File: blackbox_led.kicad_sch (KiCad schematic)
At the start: 26 parts

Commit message: refactor labels U and assigned resistance footprint
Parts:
- D10, D11, D12, D3, D4, D5: value LED -> NCD0603R3
- D6: renamed from D8; value LED -> NCD0603R3
- D7: renamed from D6; value LED -> NCD0603R3
- D8: renamed from D7; value LED -> NCD0603R3
- D9: renamed from D13; value LED -> NCD0603R3
- R28, R29, R30, R31, R32, R33, R34, R35, R36, R37, R38, R39: footprint (none) -> Resistor_SMD:R_0603_1608Metric
- U9: renamed from U10; value ~ -> CSNP1GCR01-BOW
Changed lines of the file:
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@@
 		(on_board yes)
 		(dnp no)
-		(fields_autoplaced yes)
-		(property "Reference" "D13"
-			(at 39.6875 80.01 0)
-			(effects
-				(font
-					(size 1.27 1.27)
-				)
-			)
-		)
-		(property "Value" "LED"
-			(at 39.6875 82.55 0)
+		(property "Reference" "D9"
+			(at 33.274 86.614 0)
+			(effects
+				(font
+					(size 1.27 1.27)
+				)
+			)
+		)
+		(property "Value" "NCD0603R3"
+			(at 48.006 86.614 0)
 			(effects
 				(font
@@
 			(project "fch7"
 				(path "/11716af6-0e6e-444b-b738-3f12da23c1a2/fc7fa8bf-8ca0-46b3-82d5-3a5223b4ca6b"
-					(reference "D13")
+					(reference "D9")
 					(unit 1)
 				)
@@
 		(dnp no)
 		(fields_autoplaced yes)
-		(property "Reference" "U10"
+		(property "Reference" "U9"
 			(at 167.005 52.07 0)
 			(effects
@@
 			)
 		)
-		(property "Value" "~"
+		(property "Value" "CSNP1GCR01-BOW"
 			(at 167.005 54.61 0)
 			(effects
@@
 			(project ""
 				(path "/11716af6-0e6e-444b-b738-3f12da23c1a2/fc7fa8bf-8ca0-46b3-82d5-3a5223b4ca6b"
-					(reference "U10")
+					(reference "U9")
 					(unit 1)
 				)
@@
 		(on_board yes)
 		(dnp no)
-		(fields_autoplaced yes)
 		(property "Reference" "D11"
-			(at 38.4175 105.41 0)
-			(effects
-				(font
-					(size 1.27 1.27)
-				)
-			)
-		)
-		(property "Value" "LED"
-			(at 38.4175 107.95 0)
+			(at 33.02 111.76 0)
+			(effects
+				(font
+					(size 1.27 1.27)
+				)
+			)
+		)
+		(property "Value" "NCD0603R3"
+			(at 47.244 111.76 0)
 			(effects
 				(font
@@
 			)
 		)
-		(property "Footprint" ""
+		(property "Footprint" "Resistor_SMD:R_0603_1608Metric"
 			(at 199.39 69.088 90)
 			(effects
@@
 		(on_board yes)
 		(dnp no)
-		(fields_autoplaced yes)
-		(property "Reference" "D6"
-			(at 39.6875 58.42 0)
-			(effects
-				(font
-					(size 1.27 1.27)
-				)
-			)
-		)
-		(property "Value" "LED"
-			(at 39.6875 60.96 0)
+		(property "Reference" "D7"
+			(at 35.052 65.024 0)
+			(effects
+				(font
+					(size 1.27 1.27)
+				)
+			)
+		)
+		(property "Value" "NCD0603R3"
+			(at 47.244 65.024 0)
 			(effects
 				(font
@@
 			(project "fch7"
 				(path "/11716af6-0e6e-444b-b738-3f12da23c1a2/fc7fa8bf-8ca0-46b3-82d5-3a5223b4ca6b"
-					(reference "D6")
+					(reference "D7")
 					(unit 1)
 				)
@@
 			)
 		)
-		(property "Footprint" ""
+		(property "Footprint" "Resistor_SMD:R_0603_1608Metric"
 			(at 199.39 65.278 90)
 			(effects
@@
 			)
 		)
-		(property "Footprint" ""
+		(property "Footprint" "Resistor_SMD:R_0603_1608Metric"
 			(at 55.88 104.648 90)
 			(effects
@@
 			)
 		)
-		(property "Footprint" ""
+		(property "Footprint" "Resistor_SMD:R_0603_1608Metric"
 			(at 146.05 61.468 90)
 			(effects
@@
 			)
 		)
-		(property "Footprint" ""
+		(property "Footprint" "Resistor_SMD:R_0603_1608Metric"
 			(at 54.61 124.968 90)
 			(effects
@@
 			)
 		)
-		(property "Footprint" ""
+		(property "Footprint" "Resistor_SMD:R_0603_1608Metric"
 			(at 55.88 48.768 90)
 			(effects
@@
 		(on_board yes)
 		(dnp no)
-		(fields_autoplaced yes)
 		(property "Reference" "D3"
-			(at 39.6875 17.78 0)
-			(effects
-				(font
-					(size 1.27 1.27)
-				)
-			)
-		)
-		(property "Value" "LED"
-			(at 39.6875 20.32 0)
+			(at 35.306 24.384 0)
+			(effects
+				(font
+					(size 1.27 1.27)
+				)
+			)
+		)
+		(property "Value" "NCD0603R3"
+			(at 48.006 24.384 0)
 			(effects
 				(font
@@
 		(on_board yes)
 		(dnp no)
-		(fields_autoplaced yes)
 		(property "Reference" "D5"
-			(at 39.6875 39.37 0)
-			(effects
-				(font
-					(size 1.27 1.27)
-				)
-			)
-		)
-		(property "Value" "LED"
-			(at 39.6875 41.91 0)
+			(at 35.306 45.974 0)
+			(effects
+				(font
+					(size 1.27 1.27)
+				)
+			)
+		)
+		(property "Value" "NCD0603R3"
+			(at 48.006 46.228 0)
 			(effects
 				(font
@@
 			)
 		)
-		(property "Footprint" ""
+		(property "Footprint" "Resistor_SMD:R_0603_1608Metric"
 			(at 55.88 27.178 90)
 			(effects
@@
 			)
 		)
-		(property "Footprint" ""
+		(property "Footprint" "Resistor_SMD:R_0603_1608Metric"
 			(at 146.05 65.278 90)
 			(effects
@@
 			)
 		)
-		(property "Footprint" ""
+		(property "Footprint" "Resistor_SMD:R_0603_1608Metric"
 			(at 199.39 72.898 90)
 			(effects
@@
 		(on_board yes)
 		(dnp no)
-		(fields_autoplaced yes)
-		(property "Reference" "D8"
-			(at 39.6875 48.26 0)
-			(effects
-				(font
-					(size 1.27 1.27)
-				)
-			)
-		)
-		(property "Value" "LED"
-			(at 39.6875 50.8 0)
+		(property "Reference" "D6"
+			(at 34.798 55.118 0)
+			(effects
+				(font
+					(size 1.27 1.27)
+				)
+			)
+		)
+		(property "Value" "NCD0603R3"
+			(at 47.752 55.118 0)
 			(effects
 				(font
@@
 			(project "fch7"
 				(path "/11716af6-0e6e-444b-b738-3f12da23c1a2/fc7fa8bf-8ca0-46b3-82d5-3a5223b4ca6b"
-					(reference "D8")
+					(reference "D6")
 					(unit 1)
 				)
@@
 			)
 		)
-		(property "Footprint" ""
+		(property "Footprint" "Resistor_SMD:R_0603_1608Metric"
 			(at 55.88 37.338 90)
 			(effects
@@
 		(on_board yes)
 		(dnp no)
-		(fields_autoplaced yes)
 		(property "Reference" "D4"
-			(at 39.6875 27.94 0)
-			(effects
-				(font
-					(size 1.27 1.27)
-				)
-			)
-		)
-		(property "Value" "LED"
-			(at 39.6875 30.48 0)
+			(at 34.798 34.036 0)
+			(effects
+				(font
+					(size 1.27 1.27)
+				)
+			)
+		)
+		(property "Value" "NCD0603R3"
+			(at 47.498 34.544 0)
 			(effects
 				(font
@@
 		(on_board yes)
 		(dnp no)
-		(fields_autoplaced yes)
-		(property "Reference" "D7"
-			(at 39.6875 69.85 0)
-			(effects
-				(font
-					(size 1.27 1.27)
-				)
-			)
-		)
-		(property "Value" "LED"
-			(at 39.6875 72.39 0)
+		(property "Reference" "D8"
+			(at 33.782 76.454 0)
+			(effects
+				(font
+					(size 1.27 1.27)
+				)
+			)
+		)
+		(property "Value" "NCD0603R3"
+			(at 48.514 76.454 0)
 			(effects
 				(font
@@
 			(project "fch7"
 				(path "/11716af6-0e6e-444b-b738-3f12da23c1a2/fc7fa8bf-8ca0-46b3-82d5-3a5223b4ca6b"
-					(reference "D7")
+					(reference "D8")
 					(unit 1)
 				)
@@
 			)
 		)
-		(property "Footprint" ""
+		(property "Footprint" "Resistor_SMD:R_0603_1608Metric"
 			(at 55.88 89.408 90)
 			(effects
@@
 		(on_board yes)
 		(dnp no)
-		(fields_autoplaced yes)
 		(property "Reference" "D10"
-			(at 39.6875 95.25 0)
-			(effects
-				(font
-					(size 1.27 1.27)
-				)
-			)
-		)
-		(property "Value" "LED"
-			(at 39.6875 97.79 0)
+			(at 34.29 101.854 0)
+			(effects
+				(font
+					(size 1.27 1.27)
+				)
+			)
+		)
+		(property "Value" "NCD0603R3"
+			(at 48.26 102.108 0)
 			(effects
 				(font
@@
 		(on_board yes)
 		(dnp no)
-		(fields_autoplaced yes)
 		(property "Reference" "D12"
-			(at 38.4175 115.57 0)
-			(effects
-				(font
-					(size 1.27 1.27)
-				)
-			)
-		)
-		(property "Value" "LED"
-			(at 38.4175 118.11 0)
+			(at 32.766 122.174 0)
+			(effects
+				(font
+					(size 1.27 1.27)
+				)
+			)
+		)
+		(property "Value" "NCD0603R3"
+			(at 44.704 124.46 0)
 			(effects
 				(font
@@
 			)
 		)
-		(property "Footprint" ""
+		(property "Footprint" "Resistor_SMD:R_0603_1608Metric"
 			(at 55.88 67.818 90)
 			(effects

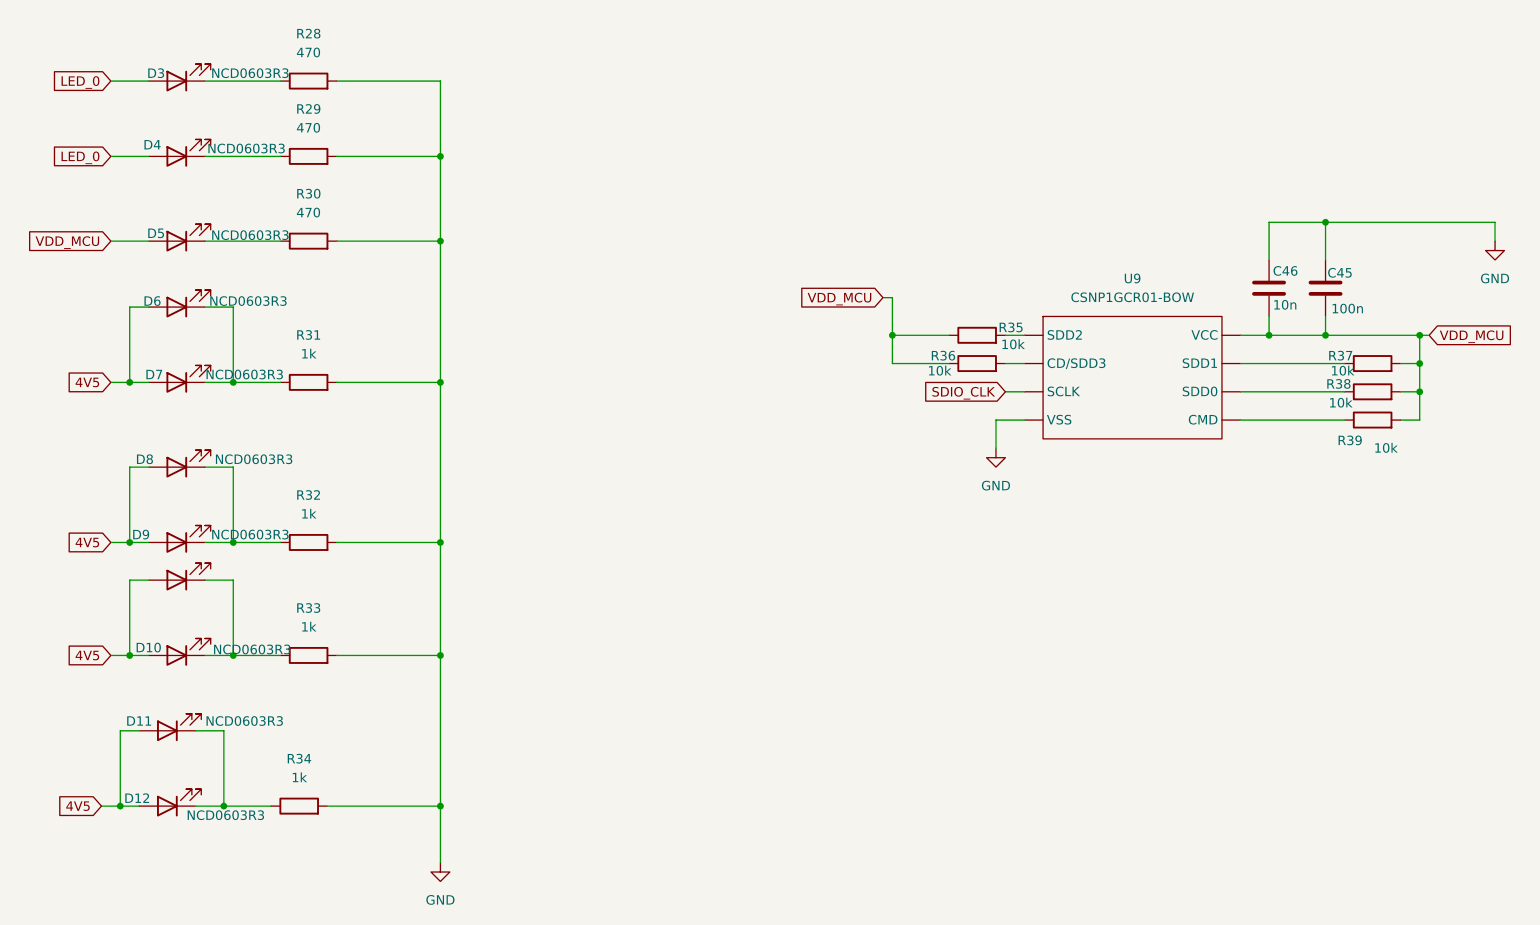
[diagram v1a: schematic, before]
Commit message: refactor and update references, added some footprints
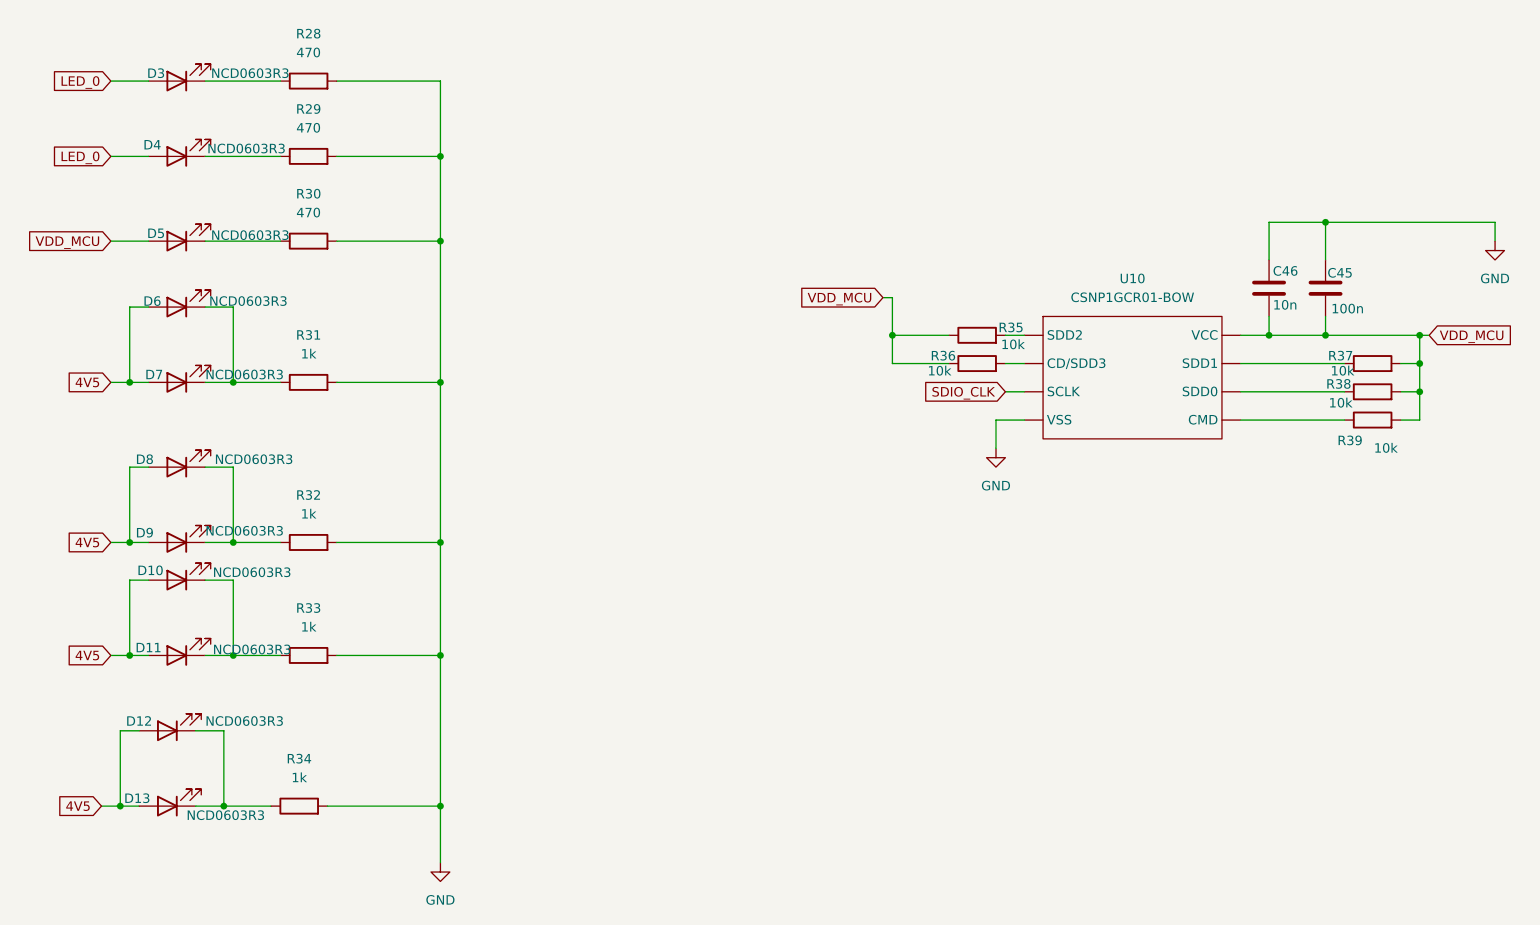
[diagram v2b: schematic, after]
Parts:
- C45, C46: footprint (none) -> Capacitor_SMD:C_0603_1608Metric
- D10: renamed from D9; value LED -> NCD0603R3; footprint (none) -> LED_SMD:LED_0603_1608Metric
- D11: renamed from D10; footprint (none) -> LED_SMD:LED_0603_1608Metric
- D12: renamed from D11; footprint (none) -> LED_SMD:LED_0603_1608Metric
- D13: renamed from D12; footprint (none) -> LED_SMD:LED_0603_1608Metric
- D3, D4, D5, D6, D7, D8, D9: footprint (none) -> LED_SMD:LED_0603_1608Metric
- renumbered U9 to U10
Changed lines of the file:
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@@
 		(dnp no)
 		(property "Reference" "D9"
-			(at 33.274 86.614 0)
+			(at 33.782 86.36 0)
 			(effects
 				(font
@@
 		)
 		(property "Value" "NCD0603R3"
-			(at 48.006 86.614 0)
-			(effects
-				(font
-					(size 1.27 1.27)
-				)
-			)
-		)
-		(property "Footprint" ""
+			(at 47.244 86.106 0)
+			(effects
+				(font
+					(size 1.27 1.27)
+				)
+			)
+		)
+		(property "Footprint" "LED_SMD:LED_0603_1608Metric"
 			(at 38.1 87.63 0)
 			(effects
@@
 		(dnp no)
 		(fields_autoplaced yes)
-		(property "Reference" "U9"
+		(property "Reference" "U10"
 			(at 167.005 52.07 0)
 			(effects
@@
 			(project ""
 				(path "/11716af6-0e6e-444b-b738-3f12da23c1a2/fc7fa8bf-8ca0-46b3-82d5-3a5223b4ca6b"
-					(reference "U9")
+					(reference "U10")
 					(unit 1)
 				)
@@
 		(on_board yes)
 		(dnp no)
-		(property "Reference" "D11"
+		(property "Reference" "D12"
 			(at 33.02 111.76 0)
 			(effects
@@
 			)
 		)
-		(property "Footprint" ""
+		(property "Footprint" "LED_SMD:LED_0603_1608Metric"
 			(at 36.83 113.03 0)
 			(effects
@@
 			(project "fch7"
 				(path "/11716af6-0e6e-444b-b738-3f12da23c1a2/fc7fa8bf-8ca0-46b3-82d5-3a5223b4ca6b"
-					(reference "D11")
+					(reference "D12")
 					(unit 1)
 				)
@@
 			)
 		)
-		(property "Footprint" ""
+		(property "Footprint" "LED_SMD:LED_0603_1608Metric"
 			(at 38.1 66.04 0)
 			(effects
@@
 			)
 		)
-		(property "Footprint" ""
+		(property "Footprint" "LED_SMD:LED_0603_1608Metric"
 			(at 38.1 25.4 0)
 			(effects
@@
 			)
 		)
-		(property "Footprint" ""
+		(property "Footprint" "LED_SMD:LED_0603_1608Metric"
 			(at 38.1 46.99 0)
 			(effects
@@
 			)
 		)
-		(property "Footprint" ""
+		(property "Footprint" "Capacitor_SMD:C_0603_1608Metric"
 			(at 194.0052 57.15 0)
 			(effects
@@
 			)
 		)
-		(property "Footprint" ""
+		(property "Footprint" "LED_SMD:LED_0603_1608Metric"
 			(at 38.1 55.88 0)
 			(effects
@@
 			)
 		)
-		(property "Footprint" ""
+		(property "Footprint" "LED_SMD:LED_0603_1608Metric"
 			(at 38.1 35.56 0)
 			(effects
@@
 			)
 		)
-		(property "Footprint" ""
+		(property "Footprint" "LED_SMD:LED_0603_1608Metric"
 			(at 38.1 77.47 0)
 			(effects
@@
 		(on_board yes)
 		(dnp no)
-		(property "Reference" "D10"
+		(property "Reference" "D11"
 			(at 34.29 101.854 0)
 			(effects
@@
 			)
 		)
-		(property "Footprint" ""
+		(property "Footprint" "LED_SMD:LED_0603_1608Metric"
 			(at 38.1 102.87 0)
 			(effects
@@
 			(project "fch7"
 				(path "/11716af6-0e6e-444b-b738-3f12da23c1a2/fc7fa8bf-8ca0-46b3-82d5-3a5223b4ca6b"
-					(reference "D10")
+					(reference "D11")
 					(unit 1)
 				)
@@
 		(on_board yes)
 		(dnp no)
-		(property "Reference" "D12"
+		(property "Reference" "D13"
 			(at 32.766 122.174 0)
 			(effects
@@
 			)
 		)
-		(property "Footprint" ""
+		(property "Footprint" "LED_SMD:LED_0603_1608Metric"
 			(at 36.83 123.19 0)
 			(effects
@@
 			(project "fch7"
 				(path "/11716af6-0e6e-444b-b738-3f12da23c1a2/fc7fa8bf-8ca0-46b3-82d5-3a5223b4ca6b"
-					(reference "D12")
+					(reference "D13")
 					(unit 1)
 				)
@@
 			)
 		)
-		(property "Footprint" ""
+		(property "Footprint" "Capacitor_SMD:C_0603_1608Metric"
 			(at 186.3852 57.15 0)
 			(effects
@@
 		(on_board yes)
 		(dnp no)
-		(fields_autoplaced yes)
-		(property "Reference" "D9"
-			(at 39.6875 85.09 0)
-			(effects
-				(font
-					(size 1.27 1.27)
-				)
-				(hide yes)
-			)
-		)
-		(property "Value" "LED"
-			(at 39.6875 87.63 0)
-			(effects
-				(font
-					(size 1.27 1.27)
-				)
-				(hide yes)
-			)
-		)
-		(property "Footprint" ""
+		(property "Reference" "D10"
+			(at 34.544 91.44 0)
+			(effects
+				(font
+					(size 1.27 1.27)
+				)
+			)
+		)
+		(property "Value" "NCD0603R3"
+			(at 48.26 91.694 0)
+			(effects
+				(font
+					(size 1.27 1.27)
+				)
+			)
+		)
+		(property "Footprint" "LED_SMD:LED_0603_1608Metric"
 			(at 38.1 92.71 0)
 			(effects
@@
 			(project "fch7"
 				(path "/11716af6-0e6e-444b-b738-3f12da23c1a2/fc7fa8bf-8ca0-46b3-82d5-3a5223b4ca6b"
-					(reference "D9")
-					(unit 1)
-				)
+					(reference "D10")
+					(unit 1)
+				)
